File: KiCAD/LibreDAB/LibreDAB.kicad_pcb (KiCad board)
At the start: 2 copper layers, 70 x 70 mm, 35 parts, among them J1 TS30050050-040, J2 TS30050050-040, J3 TS30050050-040, J4 TS30050050-040, J5 PZ254VS-11-03P-B01, J6 PZ254VS-11-03P-B01, J7 PZ254VS-11-03P-B01, Q1 SP010N01BGHTO, Q2 SP010N01BGHTO, Q3 SP010N01BGHTO, Q4 SP010N01BGHTO

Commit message: Added WIP Gate Driver
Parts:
- moved LOGO1 4.21 mm to (199.0, 111.0)
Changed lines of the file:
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@@
 	(footprint "1Footprints:FFE_Logo_12x12mm_Silk"
 		(layer "F.Cu")
-		(at 203.209616 111)
+		(at 199 111)
 		(property "Reference" "LOGO1"
 			(at -0.79 -6.73 0)

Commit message: Gate Drive schematic and footprints added
This is the last commit before trying the combined gate drive and sensing on the power board.
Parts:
- added C4: 4.7uF 50V X7S 0805, lcsc_footprints:C3861036_C0805, F.Cu at (60.4, 94.4)
- added C5: 100nF 250V X7R 0805, lcsc_footprints:C5182461_C0805, F.Cu at (60.4, 97.3)
- added J8: 1x3 Socket header, lcsc_footprints:C46635839_HDR-SMD_3P-P2_54-V-F-LS4_7-6779753103411-RC, F.Cu at (43.5, 89.5)
- added R10: 10kΩ ±1% 0805, lcsc_footprints:C2907219_R0805, F.Cu at (203.0, 72.5)
- added R11: 10kΩ ±1% 0805, lcsc_footprints:C2907219_R0805, F.Cu at (203.0, 100.5)
- added R12: 3.3Ω ±5% 1W 2512, lcsc_footprints:C393074_RES-SMD_L6_4-W3_2-1, F.Cu at (56.6, 75.9)
- added R13: 3.3Ω ±5% 1W 2512, lcsc_footprints:C393074_RES-SMD_L6_4-W3_2-1, F.Cu at (56.6, 81.3)
- added R14: 10kΩ ±1% 0805, lcsc_footprints:C2907219_R0805, F.Cu at (188.5, 72.5)
- added R15: 10kΩ ±1% 0805, lcsc_footprints:C2907219_R0805, F.Cu at (188.5, 100.5)
- added R8: 3.3Ω ±5% 1W 2512, lcsc_footprints:C393074_RES-SMD_L6_4-W3_2-1, F.Cu at (56.6, 65.0)
- added R9: 3.3Ω ±5% 1W 2512, lcsc_footprints:C393074_RES-SMD_L6_4-W3_2-1, F.Cu at (56.6, 70.4)
- added U1: UCC27211DDAR, lcsc_footprints:C141980_SOIC-8_L4_9-W3_9-P1_27-LS6_0-BL-EP, F.Cu at (54.8, 97.1)

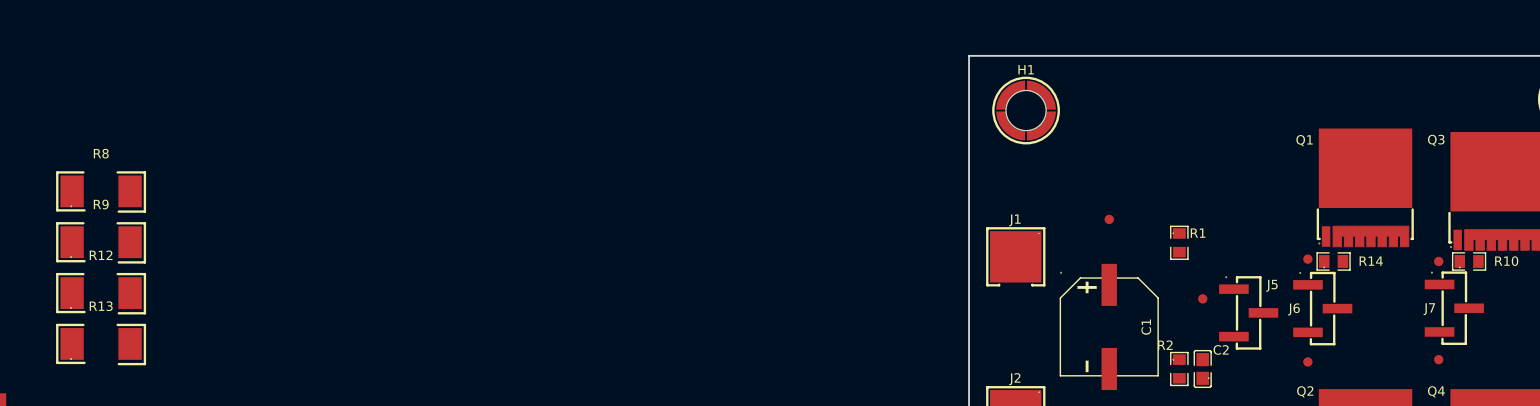
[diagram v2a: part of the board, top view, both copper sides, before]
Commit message: Edits to gate drive circuitry
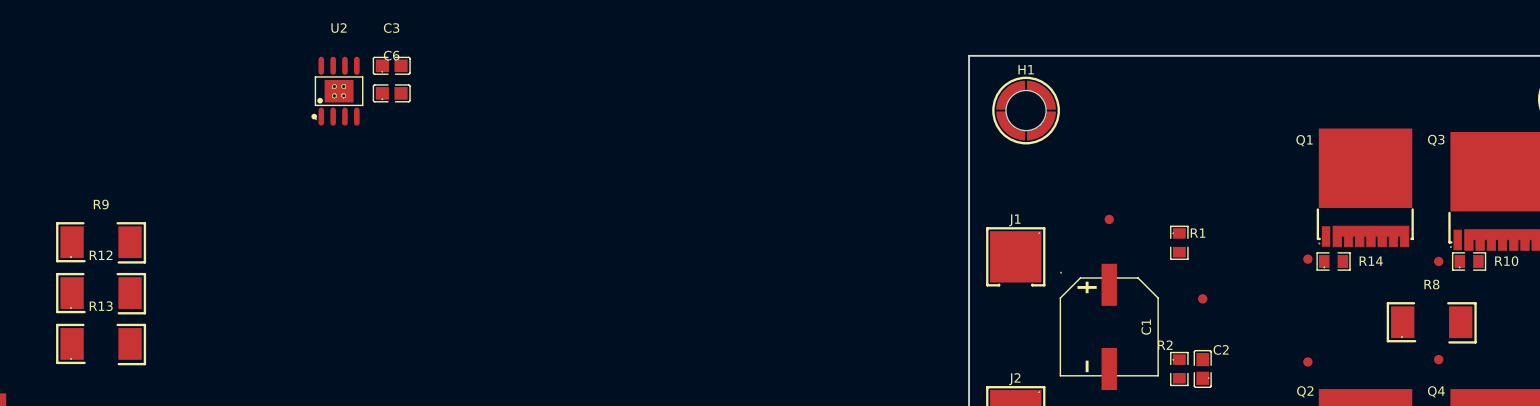
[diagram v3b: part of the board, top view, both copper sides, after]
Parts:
- removed J5, J6, J7: PZ254VS-11-03P-B01, lcsc_footprints:C41432921_HDR-SMD_3P-P2_54-V-M-LS4_8_R2
- added C3: 4.7uF 50V X7S 0805, lcsc_footprints:C3861036_C0805, F.Cu at (87.7, 51.6)
- added C6: 100nF 250V X7R 0805, lcsc_footprints:C5182461_C0805, F.Cu at (87.7, 54.5)
- added U2: UCC27211DDAR, lcsc_footprints:C141980_SOIC-8_L4_9-W3_9-P1_27-LS6_0-BL-EP, F.Cu at (82.1, 54.3)
- moved R8 143.0 mm to (199.0, 79.0)
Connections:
- net /LV_Bridge/Gate_Driver/+12V renamed /LV_Bridge/Gate_Driver1/+12V
- net /LV_Bridge/Gate_Driver/0 V renamed /LV_Bridge/Gate_Driver1/0 V
- net /LV_Bridge/Gate_Driver/PWM-H renamed /LV_Bridge/Gate_Driver1/PWM-H
- net /LV_Bridge/Gate_Driver/PWM-L renamed /LV_Bridge/Gate_Driver1/PWM-L
- net Net-(Q3-S) renamed /LV_Bridge/LSW2
- C5 pad 2: /LV_Bridge/Gate_Driver/MID -> (no net)
- J4 pad 1: Net-(Q1-S) -> /LV_Bridge/LSW1
- J8 pad 1: /LV_Bridge/Gate_Driver/QH-G -> /LV_Bridge/Gate_Driver1/QH-G
- J8 pad 2: /LV_Bridge/Gate_Driver/MID -> /LV_Bridge/Gate_Driver1/MID
- J8 pad 3: /LV_Bridge/Gate_Driver/QL-G -> /LV_Bridge/Gate_Driver1/QL-G
- Q1 pad 2: Net-(Q1-S) -> /LV_Bridge/LSW1
- Q2 pad 3: Net-(Q1-S) -> /LV_Bridge/LSW1
- R12 pad 1: Net-(J6-Pad1) -> (no net)
- R13 pad 1: Net-(J6-Pad3) -> (no net)
- R14 pad 2: Net-(Q1-S) -> /LV_Bridge/LSW1
- R8 pad 1: Net-(J7-Pad1) -> (no net)
- R9 pad 1: Net-(J7-Pad3) -> (no net)
- TP10 pad 1: Net-(Q4-G) -> /LV_Bridge/LO2
- TP6 pad 1: Net-(Q1-S) -> /LV_Bridge/LSW1
- TP7 pad 1: Net-(Q1-G) -> /LV_Bridge/HO1
- TP8 pad 1: Net-(Q2-G) -> /LV_Bridge/LO1
- TP9 pad 1: Net-(Q3-G) -> /LV_Bridge/HO2
- U1 pad 3: /LV_Bridge/Gate_Driver/QH-G -> /LV_Bridge/HO1
- U1 pad 4: /LV_Bridge/Gate_Driver/MID -> /LV_Bridge/LSW1
- U1 pad 8: /LV_Bridge/Gate_Driver/QL-G -> /LV_Bridge/LO1

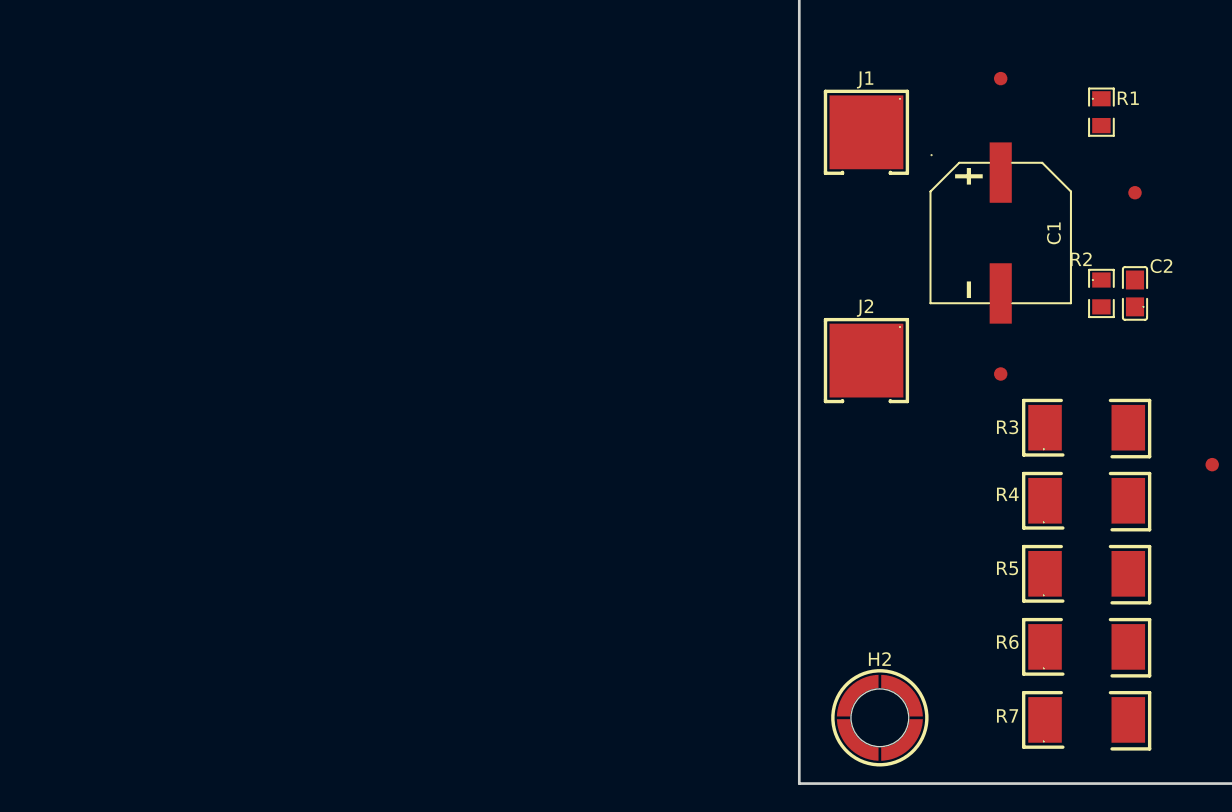
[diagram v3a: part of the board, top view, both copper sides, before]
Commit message: Added multi-pad current sense resistor footprint
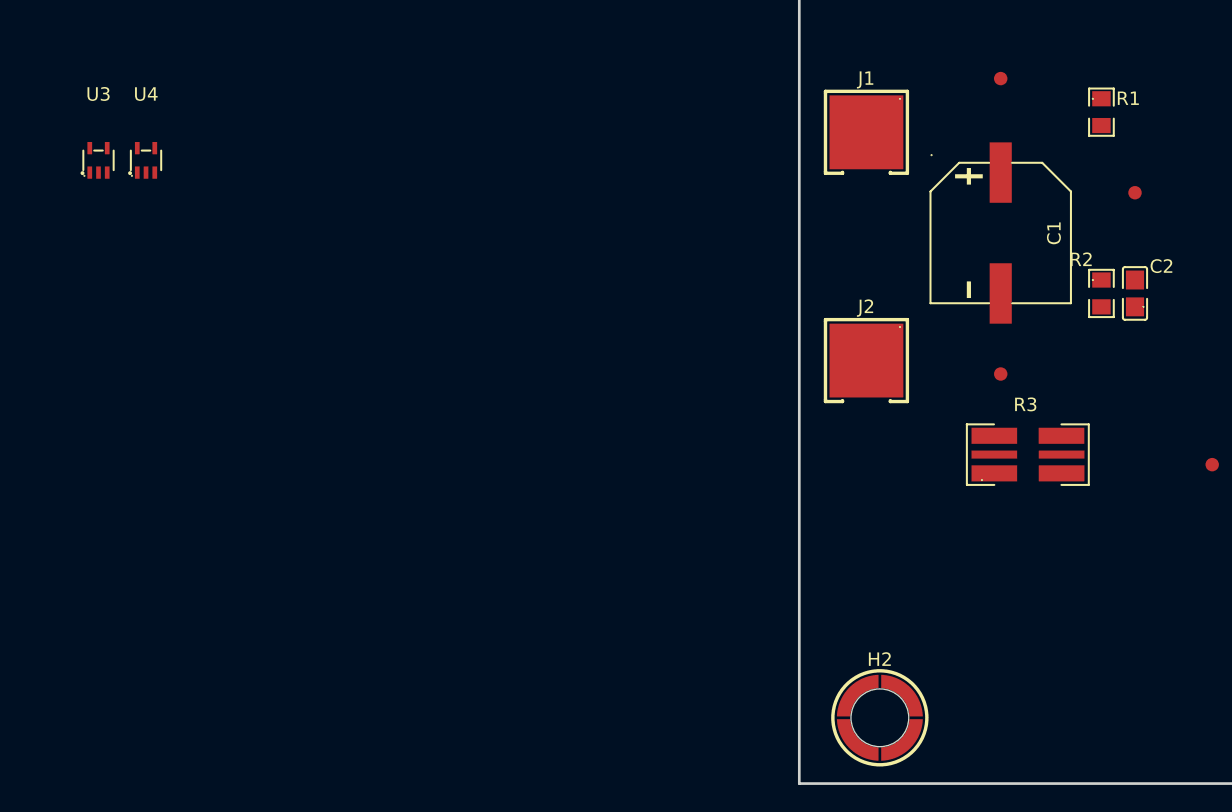
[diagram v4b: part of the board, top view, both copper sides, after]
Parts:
- removed R4, R5, R6, R7: 5mΩ ±1% 3W 2512, lcsc_footprints:C393074_RES-SMD_L6_4-W3_2-1
- added U3: MCP6486UT-E/LT, lcsc_footprints:C5224800_SC-70-5_L2_1-W1_3-P0_65-LS2_3-BL, F.Cu at (97.3, 74.1)
- added U4: MCP6486UT-E/LT, lcsc_footprints:C5224800_SC-70-5_L2_1-W1_3-P0_65-LS2_3-BL, F.Cu at (100.8, 74.1)
- R3: value 5mΩ ±1% 3W 2512 -> 0.5mΩ ±1% 3W 2512; footprint lcsc_footprints:C393074_RES-SMD_L6_4-W3_2-1 -> lcsc_footprints:C710260_RES-SMD_L6_4-W3_2_RLM25
- moved R3 4.83 mm to (166.5, 96.0)
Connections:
- net Net-(C1-Pad2) renamed /LV_Bridge/V_LV-
- net Net-(C2-Pad2) renamed /LV_Bridge/V_LV_Divider
- net Net-(Q1-D) renamed /LV_Bridge/V_LV+
- net Net-(Q2-S) renamed GND
- C5 pad 2: (no net) -> /LV_Bridge/LSW1
- C6 pad 2: (no net) -> /LV_Bridge/LSW2
- R12 pad 1: (no net) -> /LV_Bridge/HO1
- R13 pad 1: (no net) -> /LV_Bridge/LO1
- R8 pad 1: (no net) -> /LV_Bridge/HO2
- R9 pad 1: (no net) -> /LV_Bridge/LO2

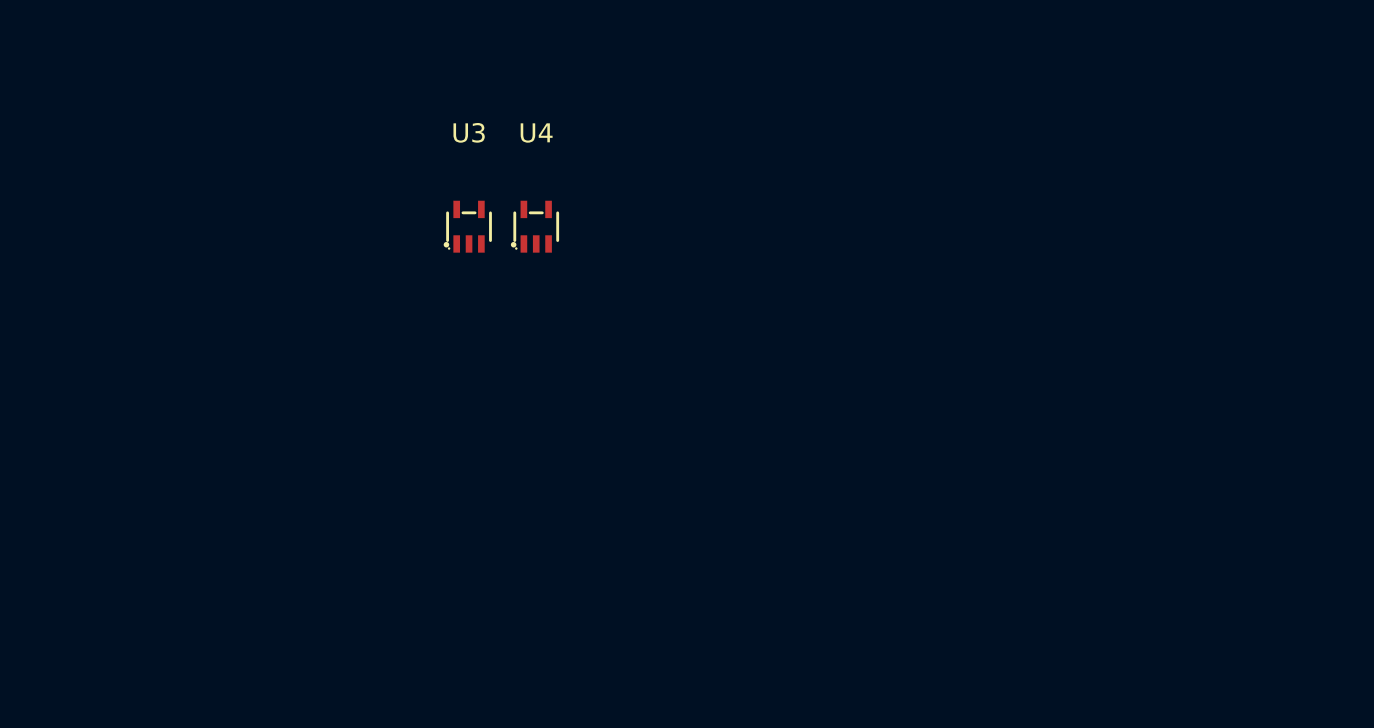
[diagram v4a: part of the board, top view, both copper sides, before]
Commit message: Added all major components to LV board
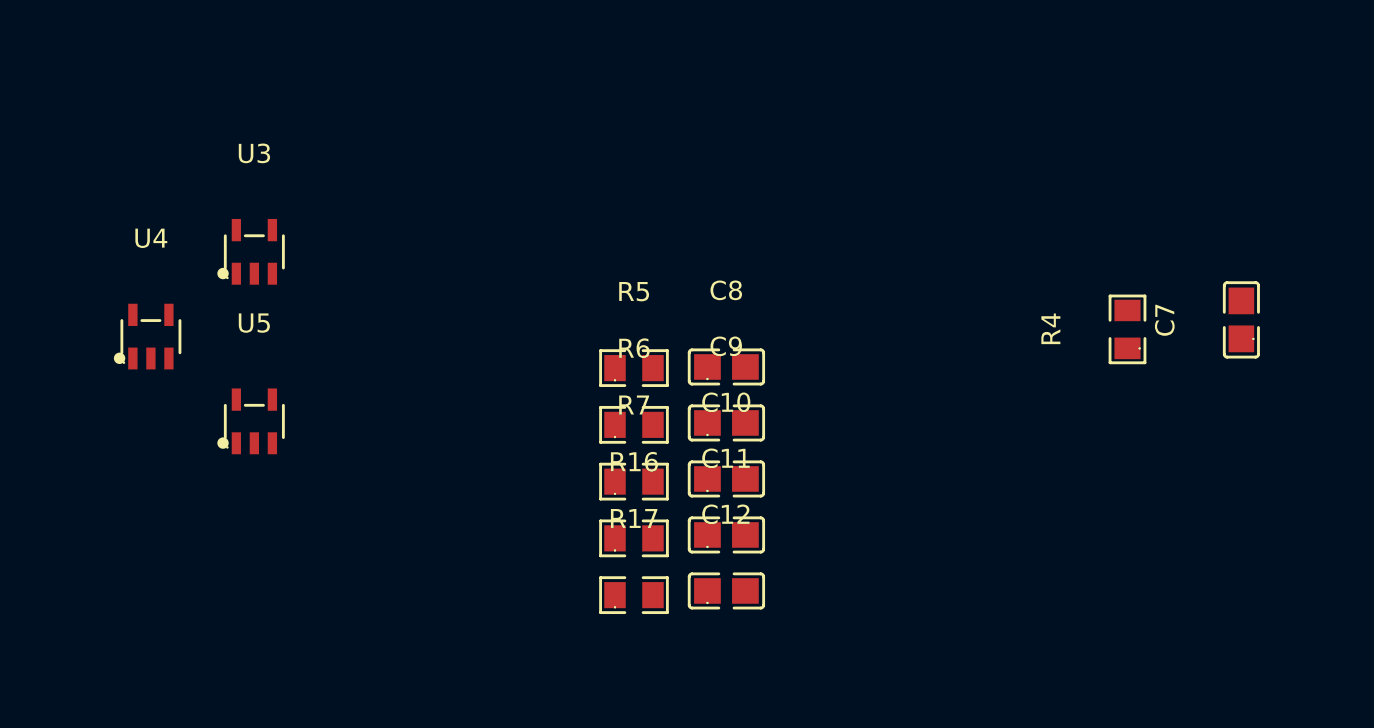
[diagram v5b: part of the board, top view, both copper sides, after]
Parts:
- added C10: 20pF 50V C0G 0805, lcsc_footprints:C176292_C0805, F.Cu at (110.9, 87.4)
- added C11: 20pF 50V C0G 0805, lcsc_footprints:C176292_C0805, F.Cu at (110.9, 90.3)
- added C12: 4.7uF 50V X7S 0805, lcsc_footprints:C3861036_C0805, F.Cu at (110.9, 93.3)
- added C7: 1nF (102) ±10% 50V, lcsc_footprints:C46653_C0805, F.Cu at (138.0, 79.0)
- added C8: 4.7uF 50V X7S 0805, lcsc_footprints:C3861036_C0805, F.Cu at (110.9, 81.5)
- added C9: 4.7uF 50V X7S 0805, lcsc_footprints:C3861036_C0805, F.Cu at (110.9, 84.4)
- added R16: 330kΩ ±0.1% 125mW 0805, lcsc_footprints:C865408_R0805, F.Cu at (106.0, 90.5)
- added R17: 330kΩ ±0.1% 125mW 0805, lcsc_footprints:C865408_R0805, F.Cu at (106.0, 93.5)
- added R4: 47kΩ ±0.1% 125mW 0805, lcsc_footprints:C2989281_R0805, F.Cu at (132.0, 79.5)
- added R5: 12.1kΩ_±0.1%_125mW_0805, lcsc_footprints:C2989281_R0805, F.Cu at (106.0, 81.5)
- added R6: 10kΩ ±0.1% 125mW 0805, lcsc_footprints:C7431042_R0805, F.Cu at (106.0, 84.5)
- added R7: 10kΩ ±0.1% 125mW 0805, lcsc_footprints:C7431042_R0805, F.Cu at (106.0, 87.5)
- added U5: 10 MHz Opamp, lcsc_footprints:C398358_SOT-23-5_L3_0-W1_7-P0_95-LS2_8-BL, F.Cu at (86.0, 84.3)
- H1, H2, H3, H4: value M3x3.5 -> MountingHole_Pad
- U3, U4: value MCP6486UT-E/LT -> 10 MHz Opamp; footprint lcsc_footprints:C5224800_SC-70-5_L2_1-W1_3-P0_65-LS2_3-BL -> lcsc_footprints:C398358_SOT-23-5_L3_0-W1_7-P0_95-LS2_8-BL
- moved U4 21.1 mm to (80.5, 79.9)
- moved U3 11.4 mm to (86.0, 75.4)
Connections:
- H1 pad 1: unconnected-(H1-Pad1) -> GND
- H2 pad 1: unconnected-(H2-Pad1) -> GND
- H3 pad 1: unconnected-(H3-Pad1) -> GND
- H4 pad 1: unconnected-(H4-Pad1) -> GND
- U3 pad 1: /LV_Bridge/V_LV_Divider -> /LV_Bridge/V_LVsense
- U3 pad 2: unconnected-(U3-VSS-Pad2) -> GND
- U3 pad 3: Net-(U3-IN-) -> /LV_Bridge/V_LV_Divider
- U3 pad 4: Net-(U3-IN-) -> /LV_Bridge/V_LVsense
- U3 pad 5: unconnected-(U3-VDD-Pad5) -> +5V
- U4 pad 1: unconnected-(U4-IN+-Pad1) -> /LV_Bridge/V_LV-
- U4 pad 2: unconnected-(U4-VSS-Pad2) -> GND
- U4 pad 3: /LV_Bridge/V_LV- -> Net-(U4-IN+)
- U4 pad 5: unconnected-(U4-VDD-Pad5) -> +5V
